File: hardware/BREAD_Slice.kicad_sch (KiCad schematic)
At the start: 15 parts, among them J1 I2C_01x04, J2 Conn_01x10_Female

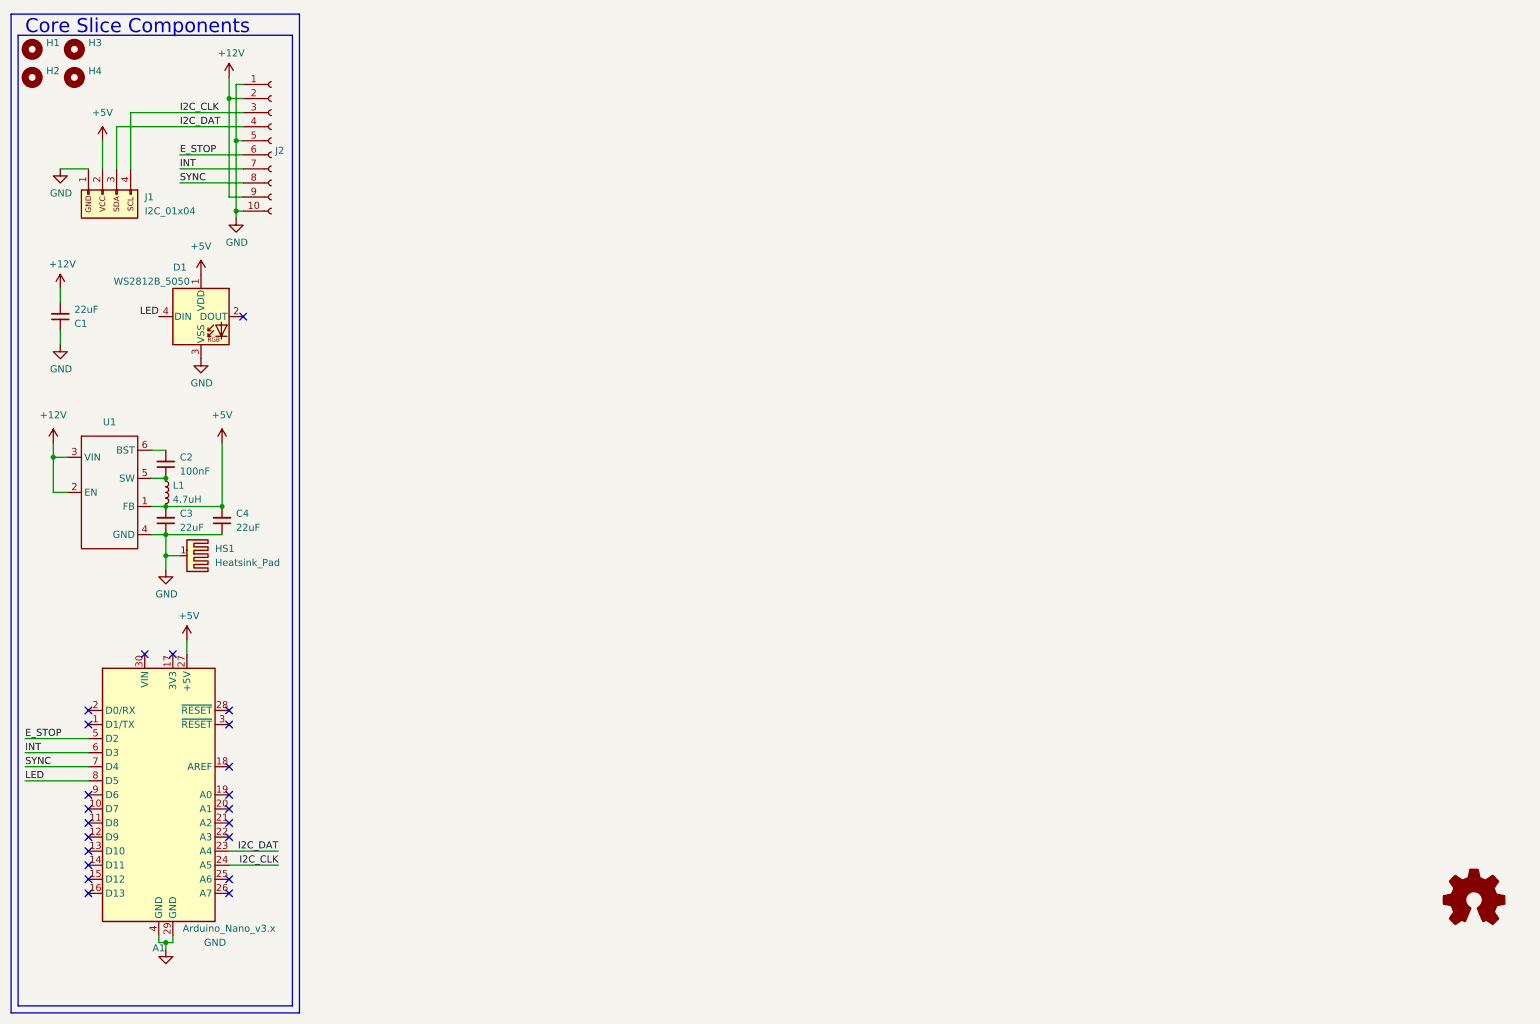
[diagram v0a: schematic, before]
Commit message: completed requirements and conceptual design, added gas sensors part of schematic for detailed design
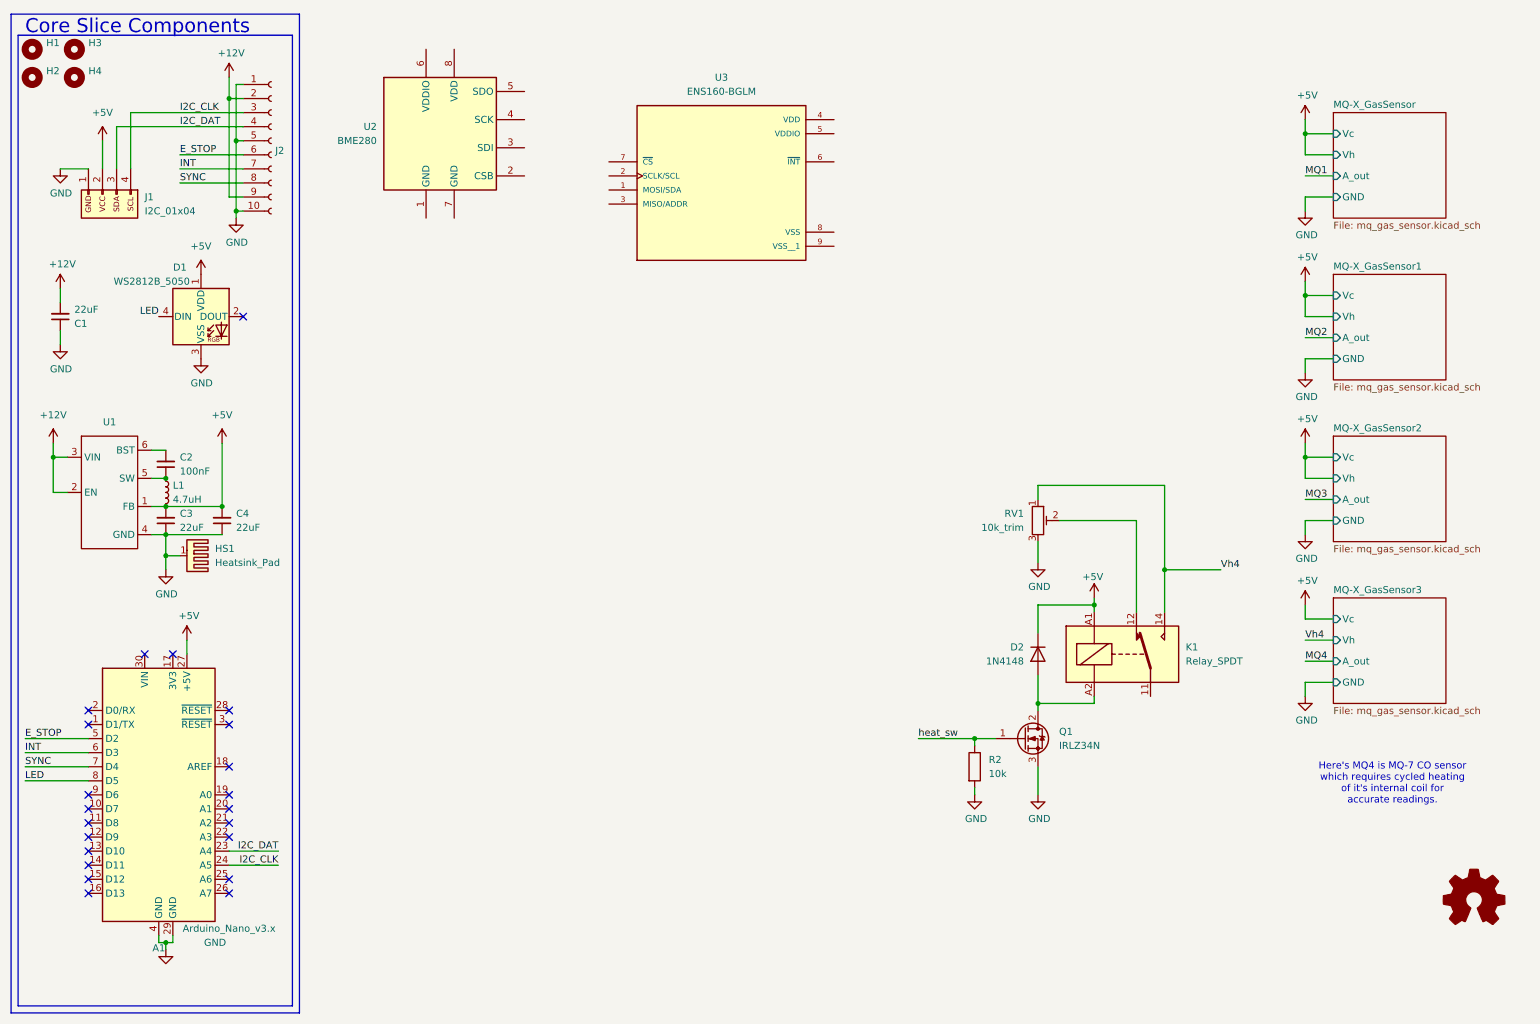
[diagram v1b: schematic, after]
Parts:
- added D2: 1N4148, Diode_THT:D_DO-35_SOD27_P7.62mm_Horizontal, symbol Diode:1N4148
- added K1: Relay_SPDT, symbol Relay:Relay_SPDT
- added Q1: IRLZ34N, Package_TO_SOT_THT:TO-220-3_Vertical, symbol Transistor_FET:IRLZ34N
- added R2: 10k, symbol Device:R
- added RV1: 10k_trim, symbol Device:R_Potentiometer_Trim
- added U2: BME280, Package_LGA:Bosch_LGA-8_2.5x2.5mm_P0.65mm_ClockwisePinNumbering, symbol Sensor:BME280
- added U3: ENS160-BGLM, ENS160-BGLM:XDCR_ENS160-BGLM, symbol kml-custom:ENS160-BGLM
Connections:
- net +5V: now also D2.1 (K), K1.A1
- net GND: now also Q1.3 (S), R2.2, RV1.3
- new net: D2.2 (A), K1.A2, Q1.2 (D)
- new net: K1.12, RV1.2
- new net Vh4: K1.14, RV1.1
- new net heat_sw: Q1.1 (G), R2.1
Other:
- added sheet MQ-X_GasSensor (mq_gas_sensor.kicad_sch)
- added sheet MQ-X_GasSensor1 (mq_gas_sensor.kicad_sch)
- added sheet MQ-X_GasSensor2 (mq_gas_sensor.kicad_sch)
- added sheet MQ-X_GasSensor3 (mq_gas_sensor.kicad_sch)
- note added: "Here's MQ4 is MQ-7 CO sensor which requires cycled heating of it's internal coil for accurate readings."

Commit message: completed schematic
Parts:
- removed RV1: 10k_trim, symbol Device:R_Potentiometer_Trim
- removed U2: BME280, Package_LGA:Bosch_LGA-8_2.5x2.5mm_P0.65mm_ClockwisePinNumbering, symbol Sensor:BME280
- removed U3: ENS160-BGLM, ENS160-BGLM:XDCR_ENS160-BGLM, symbol kml-custom:ENS160-BGLM
- added BZ1: Buzzer, symbol Device:Buzzer
- added D2: LED, symbol Device:LED
- added R1: R, symbol Device:R
- renumbered D2 to D3
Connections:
- net +5V: now also K1.12
- net GND: now also BZ1.2 (-), D2.1 (K)
- net MQ1: now also A1.19 (A0)
- net MQ2: now also A1.20 (A1)
- net MQ3: now also A1.21 (A2)
- net MQ4: now also A1.22 (A3)
- net Vh4: now also K1.11; no longer K1.14
- net heat_sw: now also A1.25 (A6)
- net ALRM_LED: now reaches A1.10 (D7)
- net ALRM_LED: now also R1.2
- net ALRM_BUZZ: now reaches A1.11 (D8)
- net ALRM_BUZZ: now also BZ1.1 (+)
- net CD: now reaches A1.12 (D9)
- net SS: now reaches A1.13 (D10)
- net DI: now reaches A1.14 (D11)
- net DO: now reaches A1.15 (D12)
- net CLK: now reaches A1.16 (D13)
- net +3V3: now reaches A1.17 (3V3)
- net CS: now reaches A1.9 (D6)
- net I2C_CLK renamed BME_SCL
- net I2C_DAT renamed BME_SDA
- new net: D2.2 (A), R1.1
- new net +1V8: K1.14
- no-connect marks 22 -> 12
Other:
- added sheet 1.8V Regulator (1V8_reg.kicad_sch)
- added sheet BME 280 (bme280.kicad_sch)
- added sheet ENS 160 (ens160.kicad_sch)
- added sheet RTC (rtc.kicad_sch)
- added sheet uSD Card Module (usd_card.kicad_sch)
- note added: "Here MQ4 is a MQ-7 CO sensor which requires cycled heating of it's internal coil for accurate readings."
- note added: "Opted for a regulator over a voltage divider since both the ENS160 and MQ-7 sensors require 1.8V, and the ENS160 application note already suggests using a regulator."
- note added: "switches between 1.8v and 5.0v"
- note removed: "Here's MQ4 is MQ-7 CO sensor which requires cycled heating of it's internal coil for accurate readings."
- moved on the sheet: D3, K1, Q1, R2

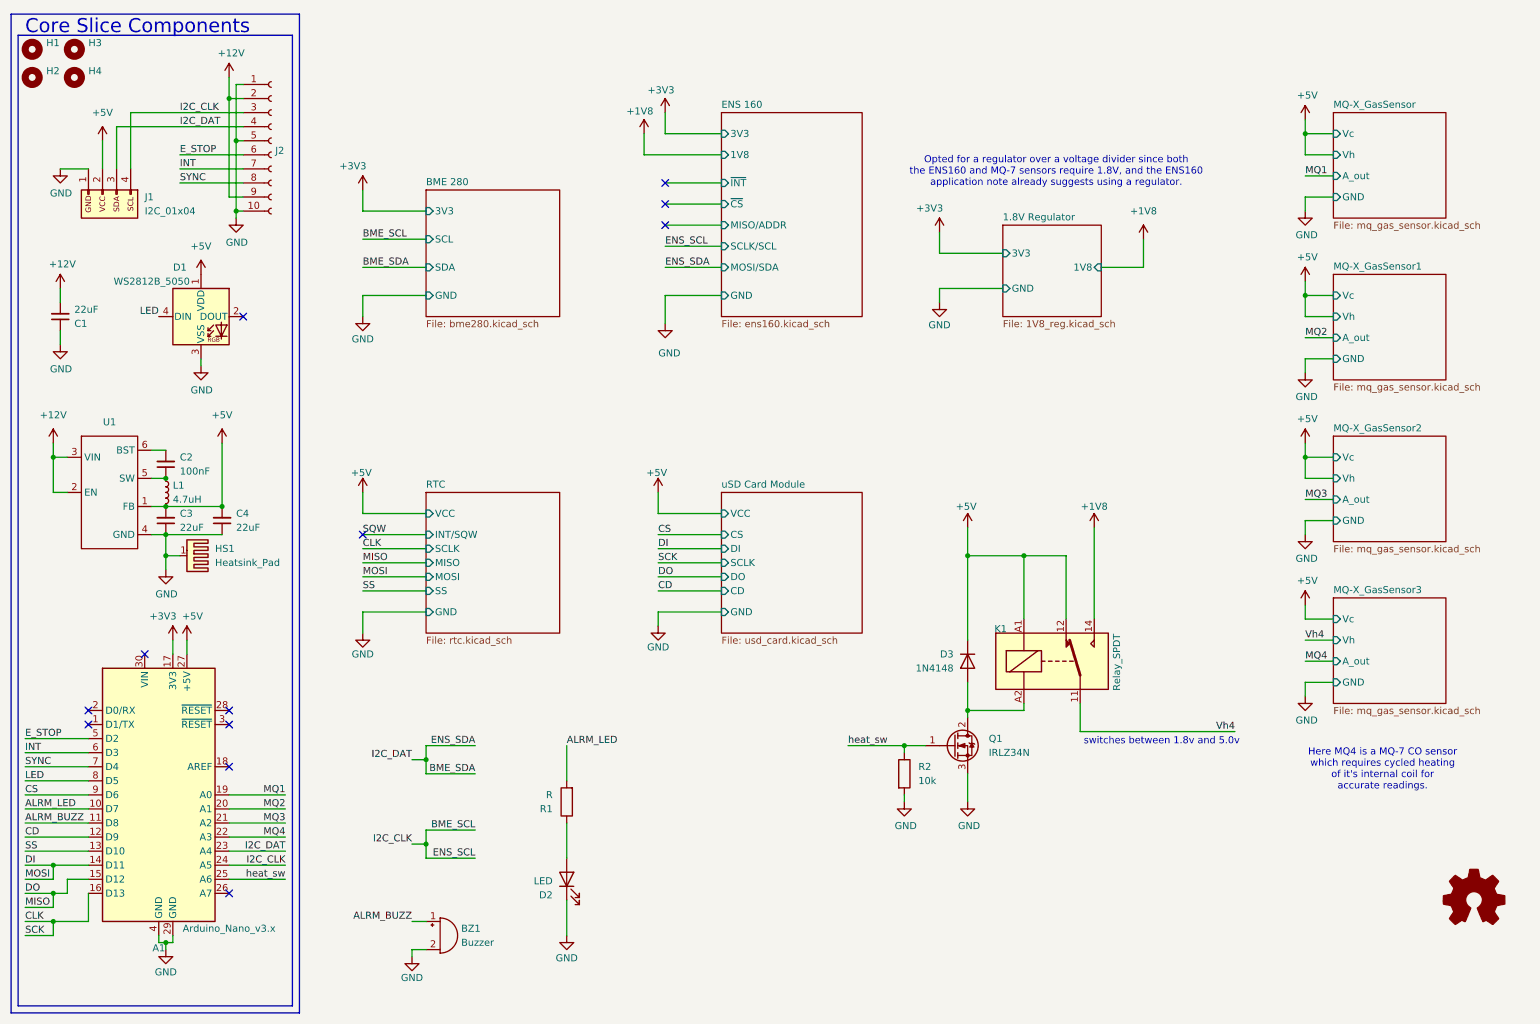
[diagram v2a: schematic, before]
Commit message: organized schem and updated readme
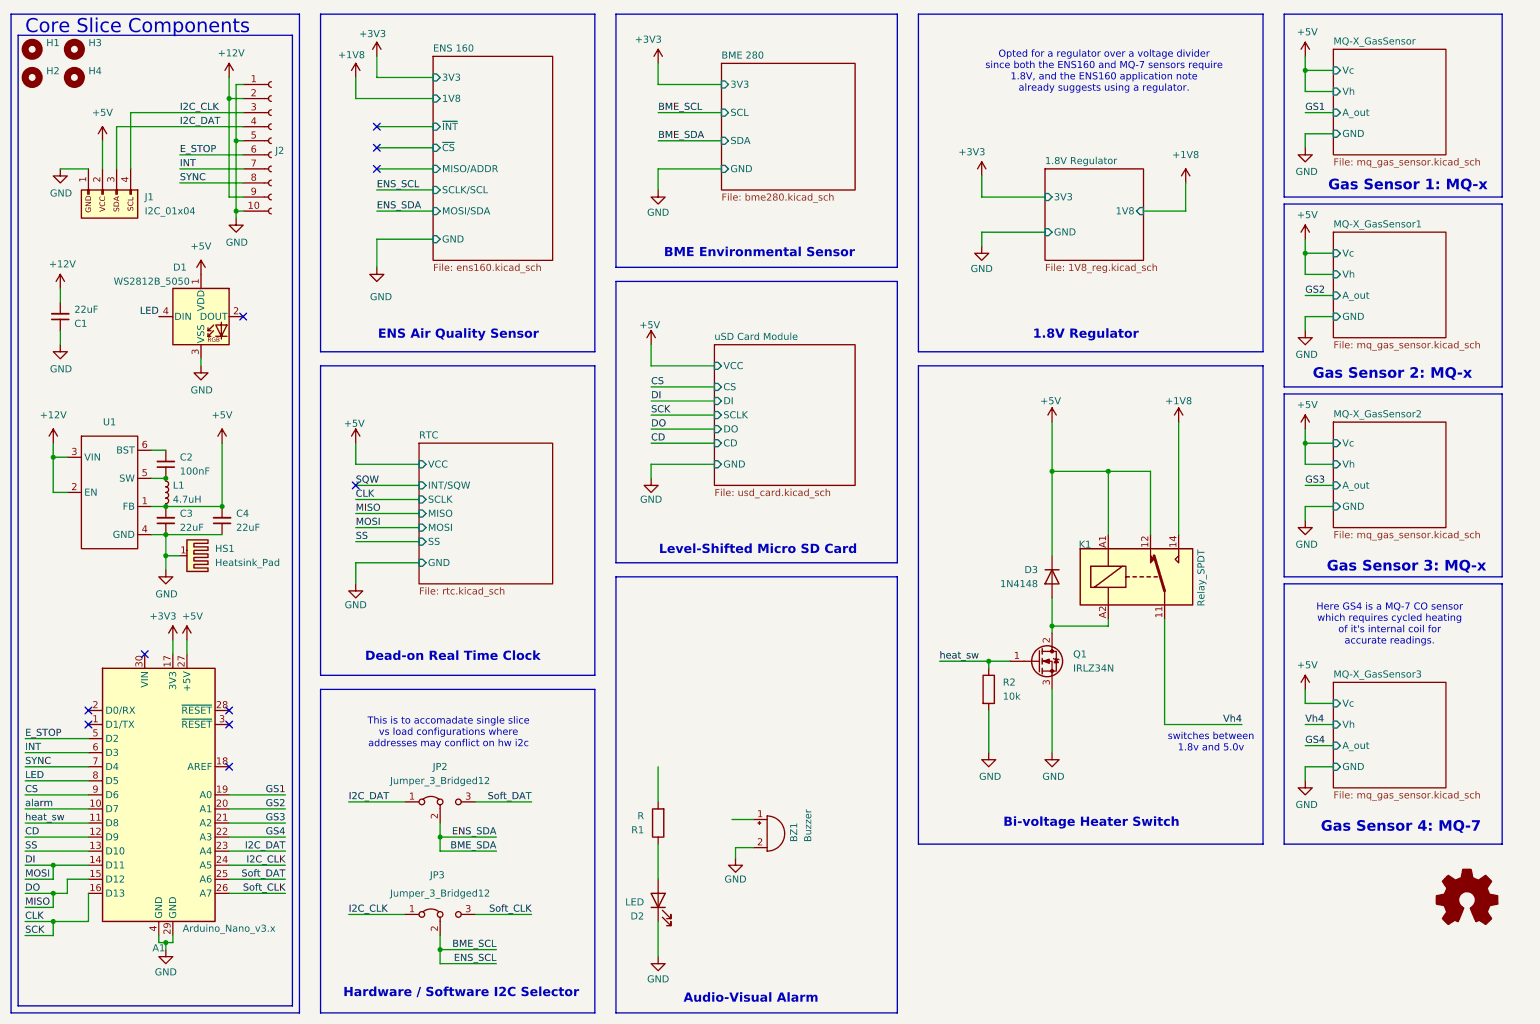
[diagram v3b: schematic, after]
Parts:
- added JP2, JP3: Jumper_3_Bridged12, symbol Jumper:Jumper_3_Bridged12
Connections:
- net BME_SCL: now also JP3.2 (C); no longer A1.24 (A5), J1.4 (Pin_4), J2.3 (Pin_3)
- net BME_SDA: now also JP2.2 (C); no longer A1.23 (A4), J1.3 (Pin_3), J2.4 (Pin_4)
- net heat_sw: now also A1.11 (D8); no longer A1.25 (A6)
- net Soft_CLK: now reaches A1.26 (A7)
- net Soft_CLK: now also JP3.3 (B)
- net ALRM_BUZZ: no longer names the net of BZ1.1 (+)
- net ALRM_BUZZ: no longer A1.11 (D8)
- net ALRM_LED: no longer names the net of R1.2
- net ALRM_LED: no longer A1.10 (D7)
- net MQ1 renamed GS1
- net MQ2 renamed GS2
- net MQ3 renamed GS3
- net MQ4 renamed GS4
- new net I2C_CLK: A1.24 (A5), J1.4 (Pin_4), J2.3 (Pin_3), JP3.1 (A)
- new net I2C_DAT: A1.23 (A4), J1.3 (Pin_3), J2.4 (Pin_4), JP2.1 (A)
- new net Soft_DAT: A1.25 (A6), JP2.3 (B)
- new net alarm: A1.10 (D7)
- no-connect marks 12 -> 11
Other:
- note added: "1.8V Regulator"
- note added: "Audio-Visual Alarm"
- note added: "BME Environmental Sensor"
- note added: "Bi-voltage Heater Switch"
- note added: "Dead-on Real Time Clock"
- note added: "ENS Air Quality Sensor"
- note added: "Gas Sensor 1: MQ-x"
- note added: "Gas Sensor 2: MQ-x"
- note added: "Gas Sensor 3: MQ-x"
- note added: "Gas Sensor 4: MQ-7"
- note added: "Hardware / Software I2C Selector"
- note added: "Here GS4 is a MQ-7 CO sensor which requires cycled heating of it's internal coil for accurate readings."
- note added: "Level-Shifted Micro SD Card"
- note added: "This is to accomadate single slice vs load configurations where addresses may conflict on hw i2c"
- note removed: "Here MQ4 is a MQ-7 CO sensor which requires cycled heating of it's internal coil for accurate readings."
- moved on the sheet: BZ1, D2, D3, K1, Q1, R1, R2

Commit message: completed board
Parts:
- removed K1: Relay_SPDT, symbol Relay:Relay_SPDT
- added D3: 1N4007, Diode_THT:D_DO-35_SOD27_P7.62mm_Horizontal, symbol Diode:1N4148
- added K2: SANYOU_SRD_Form_C, Relay_THT:Relay_SPDT_SANYOU_SRD_Series_Form_C, symbol Relay:SANYOU_SRD_Form_C
- added Q1: IRLZ34N, Package_TO_SOT_THT:TO-220-3_Horizontal_TabDown, symbol Transistor_FET:IRLZ34N
- added R2, R5: 220, Resistor_SMD:R_1206_3216Metric_Pad1.30x1.75mm_HandSolder, symbol Device:R
- added R3: 10k, Resistor_SMD:R_1206_3216Metric_Pad1.30x1.75mm_HandSolder, symbol Device:R
- BZ1: value Buzzer -> CX-1612C; footprint (none) -> Buzzer_Beeper:Buzzer_15x7.5RM7.6
- D2: value LED -> H178CAD; footprint (none) -> KML-Custom:H178CAD_P2.54mm_RightAngle_LED
- JP1: renamed from JP2; footprint (none) -> Jumper:SolderJumper-3_P1.3mm_Bridged2Bar12_Pad1.0x1.5mm_NumberLabels
- JP2: renamed from JP3; footprint (none) -> Jumper:SolderJumper-3_P1.3mm_Bridged2Bar12_Pad1.0x1.5mm_NumberLabels
- Q2: renamed from Q1; footprint Package_TO_SOT_THT:TO-220-3_Vertical -> Package_TO_SOT_THT:TO-220-3_Horizontal_TabDown
- R1: value R -> 85; footprint (none) -> Resistor_SMD:R_1206_3216Metric_Pad1.30x1.75mm_HandSolder
- R4: renamed from R2; footprint (none) -> Resistor_SMD:R_1206_3216Metric_Pad1.30x1.75mm_HandSolder
- renumbered D3 to D4
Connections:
- net +12V: now also BZ1.1 (+), D3.2 (A)
- net +1V8: now also K2.3
- net +5V: now also K2.4, K2.5
- net GND: now also Q1.3 (S), R3.2; no longer BZ1.2 (-)
- net GS1: now also A1.22 (A3); no longer A1.19 (A0)
- net GS2: now also A1.21 (A2); no longer A1.20 (A1)
- net GS3: now also A1.20 (A1); no longer A1.21 (A2)
- net GS4: now also A1.19 (A0); no longer A1.22 (A3)
- net Soft_CLK: now also A1.25 (A6); no longer A1.26 (A7)
- net Soft_DAT: now also A1.26 (A7); no longer A1.25 (A6)
- net Vh4: now also K2.1
- net alarm: now also R1.2, R2.2
- net heat_sw: now also R5.2; no longer Q2.1 (G)
- net at D4.2 (A), Q2.2 (D): now also K2.2
- new net: Q1.1 (G), R2.1, R3.1
- new net: BZ1.2 (-), D3.1 (K), Q1.2 (D)
- new net: Q2.1 (G), R5.1
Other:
- note added: "10k pulldowm R clamps to 0v when alarm low 220 gate R limits in-rush current"
- note added: "10k pulldowm R clamps to 0v when heat_sw low 220 gate R limits in-rush current"
- note added: "LED is 2V fwd, 20 mA rated (5v - 2v) / 150ohm = 20 mA"
- note added: "to prevent back emf from buzzer"
- moved on the sheet: BZ1, D4, Q2, R4
